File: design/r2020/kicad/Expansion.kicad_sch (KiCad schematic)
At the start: 31 parts, among them IC7 74LS148, J3 Conn_02x32_Odd_Even, J5 PWR, J6 Conn_01x04_Male

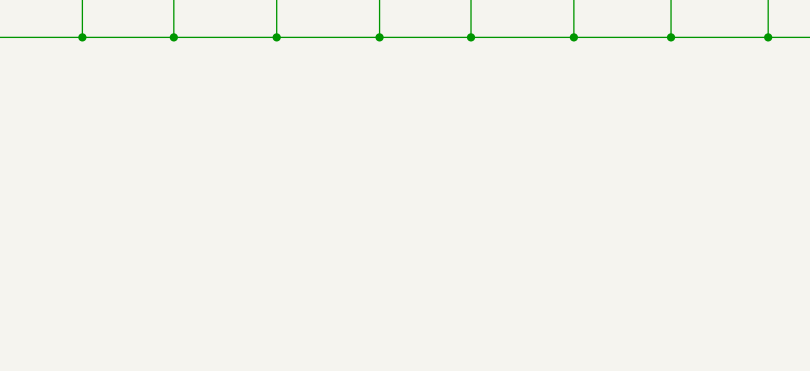
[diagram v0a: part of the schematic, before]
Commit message: Add HALT/RESET header J3X
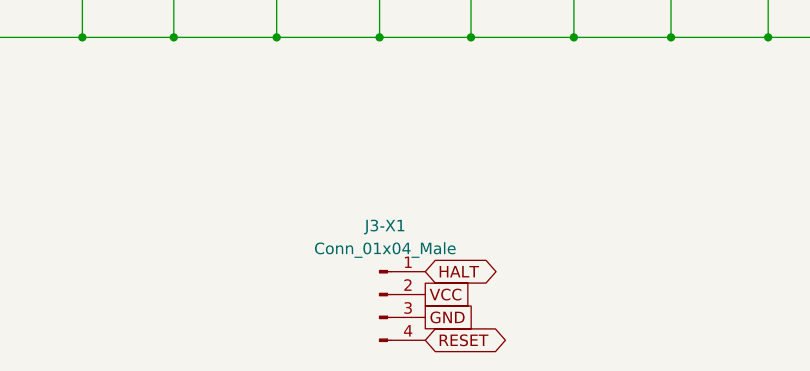
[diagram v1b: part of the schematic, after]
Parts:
- added J3-X1: Conn_01x04_Male, Connector_PinHeader_2.54mm:PinHeader_1x04_P2.54mm_Vertical, symbol Connector:Conn_01x04_Male
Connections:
- net GND: now also J3-X1.3 (Pin_3)
- net RESET: now also J3-X1.4 (Pin_4)
- net VCC: now also J3-X1.2 (Pin_2)
- new net HALT: J3-X1.1 (Pin_1)
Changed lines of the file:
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@@
+    )
+  )
+  (global_label "RESET" (shape bidirectional) (at 90.17 179.705 0) (fields_autoplaced)
+    (effects (font (size 1.27 1.27)) (justify left))
+    (property "Intersheet References" "${INTERSHEET_REFS}" (id 0) (at 98.2394 179.6256 0)
+      (effects (font (size 1.27 1.27)) (justify left) hide)
     )
   )
@@
     )
   )
+  (global_label "GND" (shape passive) (at 90.17 177.165 0) (fields_autoplaced)
+    (effects (font (size 1.27 1.27)) (justify left))
+    (property "Intersheet References" "${INTERSHEET_REFS}" (id 0) (at 96.3647 177.0856 0)
+      (effects (font (size 1.27 1.27)) (justify left) hide)
+    )
+  )
   (global_label "IPL1" (shape output) (at 173.99 60.96 0) (fields_autoplaced)
     (effects (font (size 1.27 1.27)) (justify left))
@@
     )
   )
+  (global_label "VCC" (shape passive) (at 90.17 174.625 0) (fields_autoplaced)
+    (effects (font (size 1.27 1.27)) (justify left))
+    (property "Intersheet References" "${INTERSHEET_REFS}" (id 0) (at 96.1228 174.5456 0)
+      (effects (font (size 1.27 1.27)) (justify left) hide)
+    )
+  )
   (global_label "A1" (shape input) (at 214.63 43.18 180) (fields_autoplaced)
     (effects (font (size 1.27 1.27)) (justify right))
@@
     (property "Intersheet References" "${INTERSHEET_REFS}" (id 0) (at 0 0 0)
       (effects (font (size 1.27 1.27)) hide)
+    )
+  )
+  (global_label "HALT" (shape bidirectional) (at 90.17 172.085 0) (fields_autoplaced)
+    (effects (font (size 1.27 1.27)) (justify left))
+    (property "Intersheet References" "${INTERSHEET_REFS}" (id 0) (at 96.909 172.1644 0)
+      (effects (font (size 1.27 1.27)) (justify left) hide)
     )
   )
@@
     (pin "1")
   )
+  (symbol (lib_id "Connector:Conn_01x04_Male") (at 85.09 174.625 0) (unit 1)
+    (in_bom yes) (on_board yes) (fields_autoplaced)
+    (property "Reference" "J3-X1" (id 0) (at 85.725 167.005 0))
+    (property "Value" "Conn_01x04_Male" (id 1) (at 85.725 169.545 0))
+    (property "Footprint" "Connector_PinHeader_2.54mm:PinHeader_1x04_P2.54mm_Vertical" (id 2) (at 85.09 174.625 0)
+      (effects (font (size 1.27 1.27)) hide)
+    )
+    (property "Datasheet" "~" (id 3) (at 85.09 174.625 0)
+      (effects (font (size 1.27 1.27)) hide)
+    )
+    (pin "1")
+    (pin "2")
+    (pin "3")
+    (pin "4")
+  )
   (symbol (lib_id "rosco_m68k-eagle-import:C2,5-3") (at 162.56 130.81 0) (unit 1)
